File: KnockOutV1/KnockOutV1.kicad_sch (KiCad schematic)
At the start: 0 parts

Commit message: Added STM_Breakout and Documentation Files
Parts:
- added U1: STM32F103C8T6, STM32F103C8T6:QFP50P900X900X160-48N, symbol STM32F103C8T6:STM32F103C8T6
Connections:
- new net VDD: U1.24 (VDD), U1.36 (VDD), U1.48 (VDD)
- new net VSS: U1.23 (VSS), U1.35 (VSS), U1.47 (VSS)

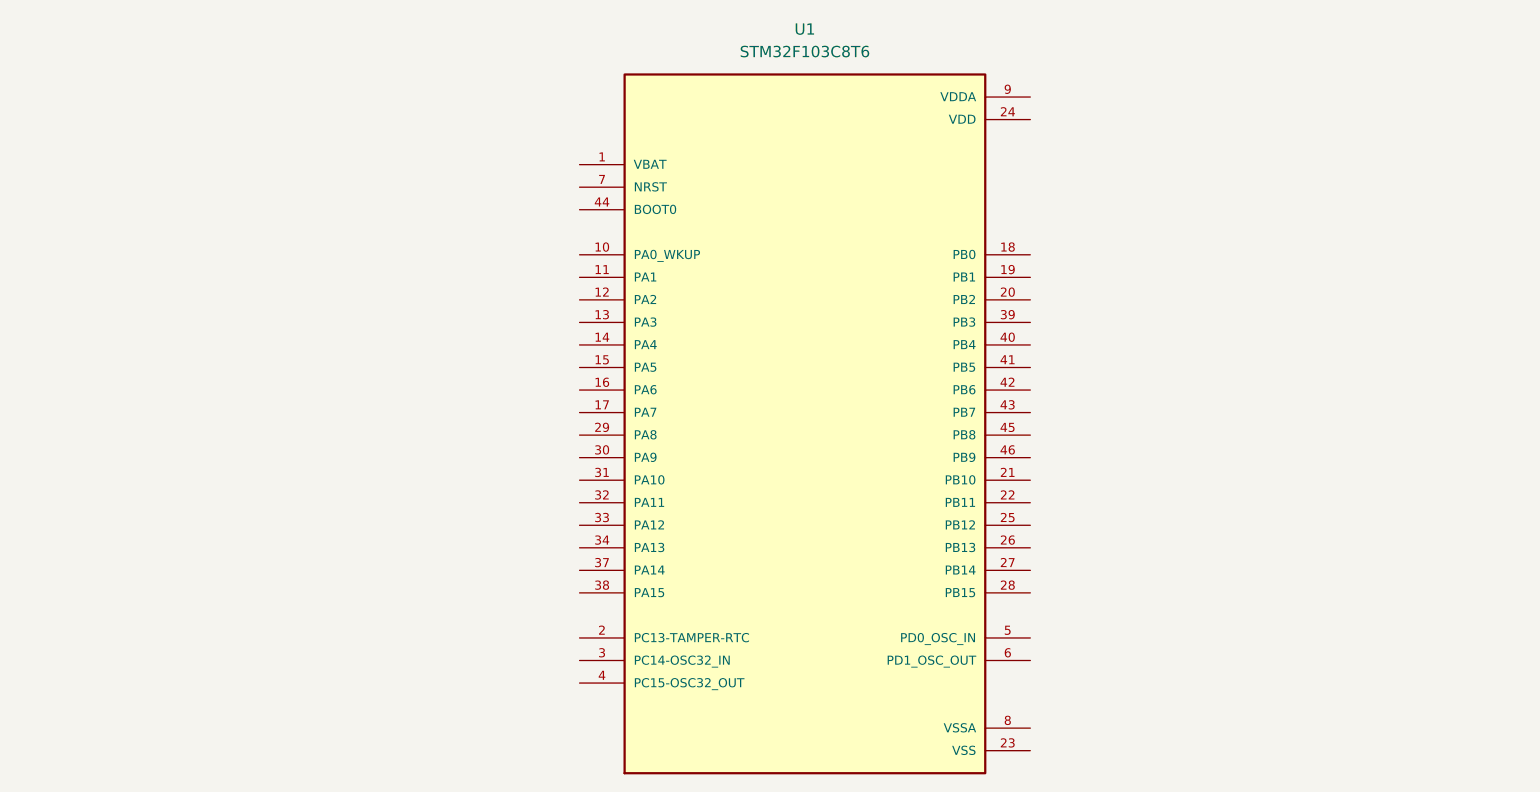
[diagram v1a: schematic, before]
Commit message: Began Schematic Pin Breakout
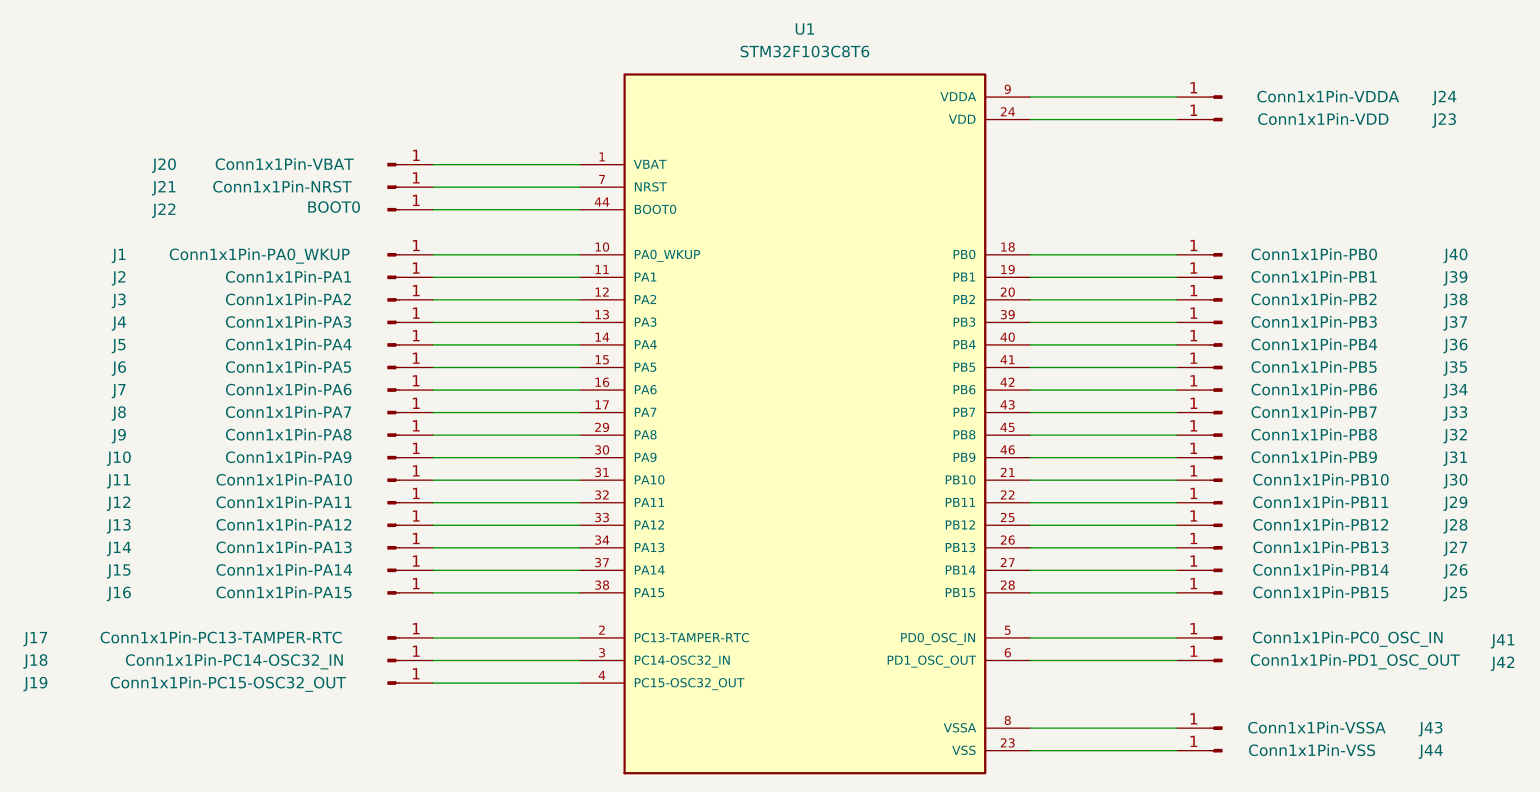
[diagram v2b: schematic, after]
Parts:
- added J1: Conn1x1Pin-PA0_WKUP, Connector_PinHeader_2.54mm:PinHeader_1x01_P2.54mm_Horizontal, symbol Connector:Conn_01x01_Pin
- added J10: Conn1x1Pin-PA9, Connector_PinHeader_2.54mm:PinHeader_1x01_P2.54mm_Horizontal, symbol Connector:Conn_01x01_Pin
- added J11: Conn1x1Pin-PA10, Connector_PinHeader_2.54mm:PinHeader_1x01_P2.54mm_Horizontal, symbol Connector:Conn_01x01_Pin
- added J12: Conn1x1Pin-PA11, Connector_PinHeader_2.54mm:PinHeader_1x01_P2.54mm_Horizontal, symbol Connector:Conn_01x01_Pin
- added J13: Conn1x1Pin-PA12, Connector_PinHeader_2.54mm:PinHeader_1x01_P2.54mm_Horizontal, symbol Connector:Conn_01x01_Pin
- added J14: Conn1x1Pin-PA13, Connector_PinHeader_2.54mm:PinHeader_1x01_P2.54mm_Horizontal, symbol Connector:Conn_01x01_Pin
- added J15: Conn1x1Pin-PA14, Connector_PinHeader_2.54mm:PinHeader_1x01_P2.54mm_Horizontal, symbol Connector:Conn_01x01_Pin
- added J16: Conn1x1Pin-PA15, Connector_PinHeader_2.54mm:PinHeader_1x01_P2.54mm_Horizontal, symbol Connector:Conn_01x01_Pin
- added J17: Conn1x1Pin-PC13-TAMPER-RTC, Connector_PinHeader_2.54mm:PinHeader_1x01_P2.54mm_Horizontal, symbol Connector:Conn_01x01_Pin
- added J18: Conn1x1Pin-PC14-OSC32_IN, Connector_PinHeader_2.54mm:PinHeader_1x01_P2.54mm_Horizontal, symbol Connector:Conn_01x01_Pin
- added J19: Conn1x1Pin-PC15-OSC32_OUT, Connector_PinHeader_2.54mm:PinHeader_1x01_P2.54mm_Horizontal, symbol Connector:Conn_01x01_Pin
- added J2: Conn1x1Pin-PA1, Connector_PinHeader_2.54mm:PinHeader_1x01_P2.54mm_Horizontal, symbol Connector:Conn_01x01_Pin
- added J20: Conn1x1Pin-VBAT, Connector_PinHeader_2.54mm:PinHeader_1x01_P2.54mm_Horizontal, symbol Connector:Conn_01x01_Pin
- added J21: Conn1x1Pin-NRST, Connector_PinHeader_2.54mm:PinHeader_1x01_P2.54mm_Horizontal, symbol Connector:Conn_01x01_Pin
- added J22: BOOT0, Connector_PinHeader_2.54mm:PinHeader_1x01_P2.54mm_Horizontal, symbol Connector:Conn_01x01_Pin
- added J23: Conn1x1Pin-VDD, Connector_PinHeader_2.54mm:PinHeader_1x01_P2.54mm_Horizontal, symbol Connector:Conn_01x01_Pin
- added J24: Conn1x1Pin-VDDA, Connector_PinHeader_2.54mm:PinHeader_1x01_P2.54mm_Horizontal, symbol Connector:Conn_01x01_Pin
- added J25: Conn1x1Pin-PB15, Connector_PinHeader_2.54mm:PinHeader_1x01_P2.54mm_Horizontal, symbol Connector:Conn_01x01_Pin
- added J26: Conn1x1Pin-PB14, Connector_PinHeader_2.54mm:PinHeader_1x01_P2.54mm_Horizontal, symbol Connector:Conn_01x01_Pin
- added J27: Conn1x1Pin-PB13, Connector_PinHeader_2.54mm:PinHeader_1x01_P2.54mm_Horizontal, symbol Connector:Conn_01x01_Pin
- added J28: Conn1x1Pin-PB12, Connector_PinHeader_2.54mm:PinHeader_1x01_P2.54mm_Horizontal, symbol Connector:Conn_01x01_Pin
- added J29: Conn1x1Pin-PB11, Connector_PinHeader_2.54mm:PinHeader_1x01_P2.54mm_Horizontal, symbol Connector:Conn_01x01_Pin
- added J3: Conn1x1Pin-PA2, Connector_PinHeader_2.54mm:PinHeader_1x01_P2.54mm_Horizontal, symbol Connector:Conn_01x01_Pin
- added J30: Conn1x1Pin-PB10, Connector_PinHeader_2.54mm:PinHeader_1x01_P2.54mm_Horizontal, symbol Connector:Conn_01x01_Pin
- added J31: Conn1x1Pin-PB9, Connector_PinHeader_2.54mm:PinHeader_1x01_P2.54mm_Horizontal, symbol Connector:Conn_01x01_Pin
- added J32: Conn1x1Pin-PB8, Connector_PinHeader_2.54mm:PinHeader_1x01_P2.54mm_Horizontal, symbol Connector:Conn_01x01_Pin
- added J33: Conn1x1Pin-PB7, Connector_PinHeader_2.54mm:PinHeader_1x01_P2.54mm_Horizontal, symbol Connector:Conn_01x01_Pin
- added J34: Conn1x1Pin-PB6, Connector_PinHeader_2.54mm:PinHeader_1x01_P2.54mm_Horizontal, symbol Connector:Conn_01x01_Pin
- added J35: Conn1x1Pin-PB5, Connector_PinHeader_2.54mm:PinHeader_1x01_P2.54mm_Horizontal, symbol Connector:Conn_01x01_Pin
- added J36: Conn1x1Pin-PB4, Connector_PinHeader_2.54mm:PinHeader_1x01_P2.54mm_Horizontal, symbol Connector:Conn_01x01_Pin
- added J37: Conn1x1Pin-PB3, Connector_PinHeader_2.54mm:PinHeader_1x01_P2.54mm_Horizontal, symbol Connector:Conn_01x01_Pin
- added J38: Conn1x1Pin-PB2, Connector_PinHeader_2.54mm:PinHeader_1x01_P2.54mm_Horizontal, symbol Connector:Conn_01x01_Pin
- added J39: Conn1x1Pin-PB1, Connector_PinHeader_2.54mm:PinHeader_1x01_P2.54mm_Horizontal, symbol Connector:Conn_01x01_Pin
- added J4: Conn1x1Pin-PA3, Connector_PinHeader_2.54mm:PinHeader_1x01_P2.54mm_Horizontal, symbol Connector:Conn_01x01_Pin
- added J40: Conn1x1Pin-PB0, Connector_PinHeader_2.54mm:PinHeader_1x01_P2.54mm_Horizontal, symbol Connector:Conn_01x01_Pin
- added J41: Conn1x1Pin-PC0_OSC_IN, Connector_PinHeader_2.54mm:PinHeader_1x01_P2.54mm_Horizontal, symbol Connector:Conn_01x01_Pin
- added J42: Conn1x1Pin-PD1_OSC_OUT, Connector_PinHeader_2.54mm:PinHeader_1x01_P2.54mm_Horizontal, symbol Connector:Conn_01x01_Pin
- added J43: Conn1x1Pin-VSSA, Connector_PinHeader_2.54mm:PinHeader_1x01_P2.54mm_Horizontal, symbol Connector:Conn_01x01_Pin
- added J44: Conn1x1Pin-VSS, Connector_PinHeader_2.54mm:PinHeader_1x01_P2.54mm_Horizontal, symbol Connector:Conn_01x01_Pin
- added J5: Conn1x1Pin-PA4, Connector_PinHeader_2.54mm:PinHeader_1x01_P2.54mm_Horizontal, symbol Connector:Conn_01x01_Pin
- added J6: Conn1x1Pin-PA5, Connector_PinHeader_2.54mm:PinHeader_1x01_P2.54mm_Horizontal, symbol Connector:Conn_01x01_Pin
- added J7: Conn1x1Pin-PA6, Connector_PinHeader_2.54mm:PinHeader_1x01_P2.54mm_Horizontal, symbol Connector:Conn_01x01_Pin
- added J8: Conn1x1Pin-PA7, Connector_PinHeader_2.54mm:PinHeader_1x01_P2.54mm_Horizontal, symbol Connector:Conn_01x01_Pin
- added J9: Conn1x1Pin-PA8, Connector_PinHeader_2.54mm:PinHeader_1x01_P2.54mm_Horizontal, symbol Connector:Conn_01x01_Pin
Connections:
- net VDD: now also J23.1 (Pin_1)
- net VSS: now also J44.1 (Pin_1)
- net at U1.1 (VBAT): now also J20.1 (Pin_1)
- net at U1.10 (PA0_WKUP): now also J1.1 (Pin_1)
- net at U1.11 (PA1): now also J2.1 (Pin_1)
- net at U1.12 (PA2): now also J3.1 (Pin_1)
- net at U1.13 (PA3): now also J4.1 (Pin_1)
- net at U1.14 (PA4): now also J5.1 (Pin_1)
- net at U1.15 (PA5): now also J6.1 (Pin_1)
- net at U1.16 (PA6): now also J7.1 (Pin_1)
- net at U1.17 (PA7): now also J8.1 (Pin_1)
- net at U1.18 (PB0): now also J40.1 (Pin_1)
- net at U1.19 (PB1): now also J39.1 (Pin_1)
- net at U1.2 (PC13-TAMPER-RTC): now also J17.1 (Pin_1)
- net at U1.20 (PB2): now also J38.1 (Pin_1)
- net at U1.21 (PB10): now also J30.1 (Pin_1)
- net at U1.22 (PB11): now also J29.1 (Pin_1)
- net at U1.25 (PB12): now also J28.1 (Pin_1)
- net at U1.26 (PB13): now also J27.1 (Pin_1)
- net at U1.27 (PB14): now also J26.1 (Pin_1)
- net at U1.28 (PB15): now also J25.1 (Pin_1)
- net at U1.29 (PA8): now also J9.1 (Pin_1)
- net at U1.3 (PC14-OSC32_IN): now also J18.1 (Pin_1)
- net at U1.30 (PA9): now also J10.1 (Pin_1)
- net at U1.31 (PA10): now also J11.1 (Pin_1)
- net at U1.32 (PA11): now also J12.1 (Pin_1)
- net at U1.33 (PA12): now also J13.1 (Pin_1)
- net at U1.34 (PA13): now also J14.1 (Pin_1)
- net at U1.37 (PA14): now also J15.1 (Pin_1)
- net at U1.38 (PA15): now also J16.1 (Pin_1)
- net at U1.39 (PB3): now also J37.1 (Pin_1)
- net at U1.4 (PC15-OSC32_OUT): now also J19.1 (Pin_1)
- net at U1.40 (PB4): now also J36.1 (Pin_1)
- net at U1.41 (PB5): now also J35.1 (Pin_1)
- net at U1.42 (PB6): now also J34.1 (Pin_1)
- net at U1.43 (PB7): now also J33.1 (Pin_1)
- net at U1.44 (BOOT0): now also J22.1 (Pin_1)
- net at U1.45 (PB8): now also J32.1 (Pin_1)
- net at U1.46 (PB9): now also J31.1 (Pin_1)
- net at U1.5 (PD0_OSC_IN): now also J41.1 (Pin_1)
- net at U1.6 (PD1_OSC_OUT): now also J42.1 (Pin_1)
- net at U1.7 (NRST): now also J21.1 (Pin_1)
- net at U1.8 (VSSA): now also J43.1 (Pin_1)
- net at U1.9 (VDDA): now also J24.1 (Pin_1)

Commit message: Rearraged Files
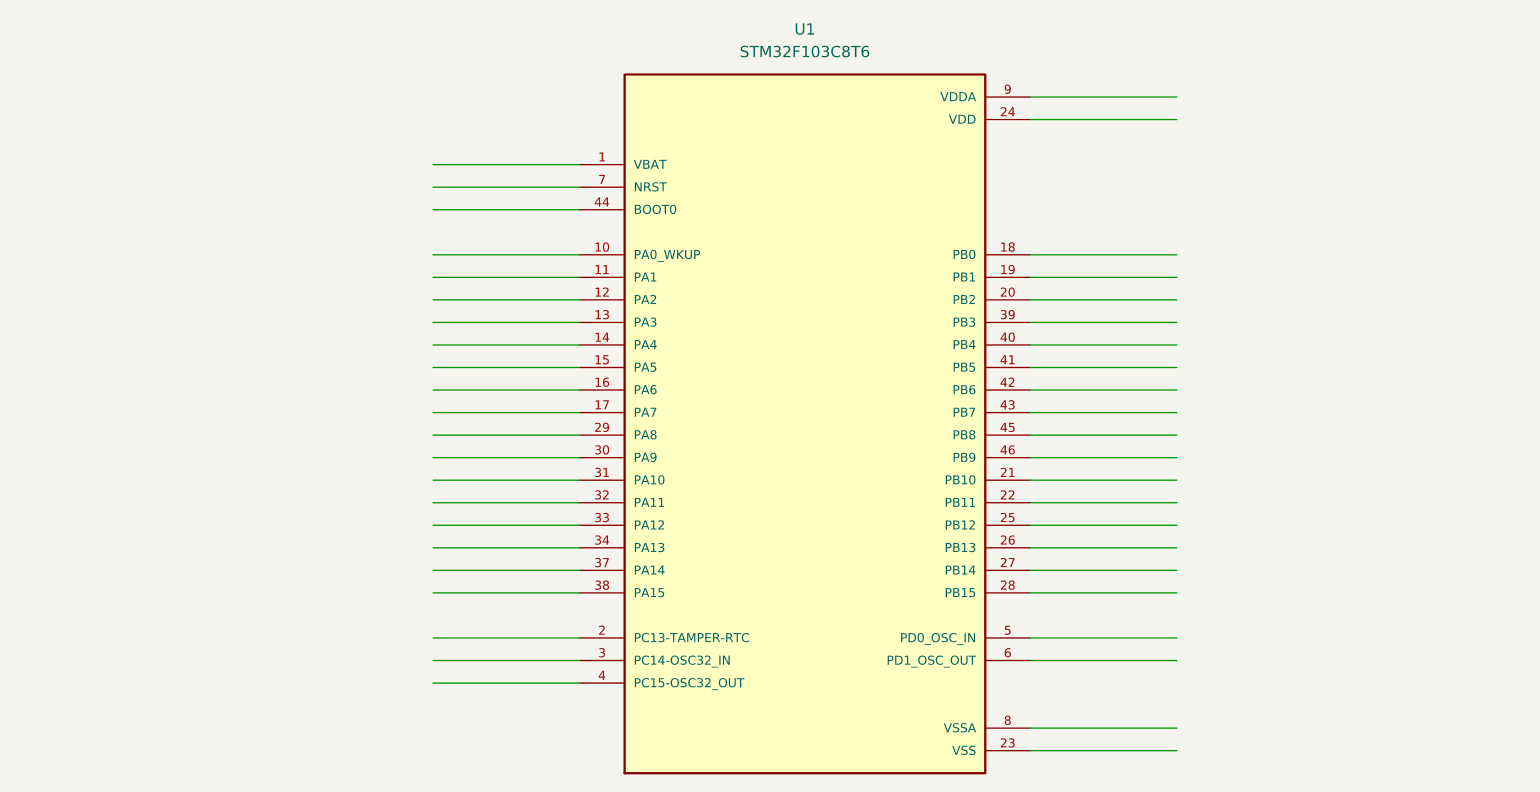
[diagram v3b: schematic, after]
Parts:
- removed J1: Conn1x1Pin-PA0_WKUP, Connector_PinHeader_2.54mm:PinHeader_1x01_P2.54mm_Horizontal, symbol Connector:Conn_01x01_Pin
- removed J10: Conn1x1Pin-PA9, Connector_PinHeader_2.54mm:PinHeader_1x01_P2.54mm_Horizontal, symbol Connector:Conn_01x01_Pin
- removed J11: Conn1x1Pin-PA10, Connector_PinHeader_2.54mm:PinHeader_1x01_P2.54mm_Horizontal, symbol Connector:Conn_01x01_Pin
- removed J12: Conn1x1Pin-PA11, Connector_PinHeader_2.54mm:PinHeader_1x01_P2.54mm_Horizontal, symbol Connector:Conn_01x01_Pin
- removed J13: Conn1x1Pin-PA12, Connector_PinHeader_2.54mm:PinHeader_1x01_P2.54mm_Horizontal, symbol Connector:Conn_01x01_Pin
- removed J14: Conn1x1Pin-PA13, Connector_PinHeader_2.54mm:PinHeader_1x01_P2.54mm_Horizontal, symbol Connector:Conn_01x01_Pin
- removed J15: Conn1x1Pin-PA14, Connector_PinHeader_2.54mm:PinHeader_1x01_P2.54mm_Horizontal, symbol Connector:Conn_01x01_Pin
- removed J16: Conn1x1Pin-PA15, Connector_PinHeader_2.54mm:PinHeader_1x01_P2.54mm_Horizontal, symbol Connector:Conn_01x01_Pin
- removed J17: Conn1x1Pin-PC13-TAMPER-RTC, Connector_PinHeader_2.54mm:PinHeader_1x01_P2.54mm_Horizontal, symbol Connector:Conn_01x01_Pin
- removed J18: Conn1x1Pin-PC14-OSC32_IN, Connector_PinHeader_2.54mm:PinHeader_1x01_P2.54mm_Horizontal, symbol Connector:Conn_01x01_Pin
- removed J19: Conn1x1Pin-PC15-OSC32_OUT, Connector_PinHeader_2.54mm:PinHeader_1x01_P2.54mm_Horizontal, symbol Connector:Conn_01x01_Pin
- removed J2: Conn1x1Pin-PA1, Connector_PinHeader_2.54mm:PinHeader_1x01_P2.54mm_Horizontal, symbol Connector:Conn_01x01_Pin
- removed J20: Conn1x1Pin-VBAT, Connector_PinHeader_2.54mm:PinHeader_1x01_P2.54mm_Horizontal, symbol Connector:Conn_01x01_Pin
- removed J21: Conn1x1Pin-NRST, Connector_PinHeader_2.54mm:PinHeader_1x01_P2.54mm_Horizontal, symbol Connector:Conn_01x01_Pin
- removed J22: BOOT0, Connector_PinHeader_2.54mm:PinHeader_1x01_P2.54mm_Horizontal, symbol Connector:Conn_01x01_Pin
- removed J23: Conn1x1Pin-VDD, Connector_PinHeader_2.54mm:PinHeader_1x01_P2.54mm_Horizontal, symbol Connector:Conn_01x01_Pin
- removed J24: Conn1x1Pin-VDDA, Connector_PinHeader_2.54mm:PinHeader_1x01_P2.54mm_Horizontal, symbol Connector:Conn_01x01_Pin
- removed J25: Conn1x1Pin-PB15, Connector_PinHeader_2.54mm:PinHeader_1x01_P2.54mm_Horizontal, symbol Connector:Conn_01x01_Pin
- removed J26: Conn1x1Pin-PB14, Connector_PinHeader_2.54mm:PinHeader_1x01_P2.54mm_Horizontal, symbol Connector:Conn_01x01_Pin
- removed J27: Conn1x1Pin-PB13, Connector_PinHeader_2.54mm:PinHeader_1x01_P2.54mm_Horizontal, symbol Connector:Conn_01x01_Pin
- removed J28: Conn1x1Pin-PB12, Connector_PinHeader_2.54mm:PinHeader_1x01_P2.54mm_Horizontal, symbol Connector:Conn_01x01_Pin
- removed J29: Conn1x1Pin-PB11, Connector_PinHeader_2.54mm:PinHeader_1x01_P2.54mm_Horizontal, symbol Connector:Conn_01x01_Pin
- removed J3: Conn1x1Pin-PA2, Connector_PinHeader_2.54mm:PinHeader_1x01_P2.54mm_Horizontal, symbol Connector:Conn_01x01_Pin
- removed J30: Conn1x1Pin-PB10, Connector_PinHeader_2.54mm:PinHeader_1x01_P2.54mm_Horizontal, symbol Connector:Conn_01x01_Pin
- removed J31: Conn1x1Pin-PB9, Connector_PinHeader_2.54mm:PinHeader_1x01_P2.54mm_Horizontal, symbol Connector:Conn_01x01_Pin
- removed J32: Conn1x1Pin-PB8, Connector_PinHeader_2.54mm:PinHeader_1x01_P2.54mm_Horizontal, symbol Connector:Conn_01x01_Pin
- removed J33: Conn1x1Pin-PB7, Connector_PinHeader_2.54mm:PinHeader_1x01_P2.54mm_Horizontal, symbol Connector:Conn_01x01_Pin
- removed J34: Conn1x1Pin-PB6, Connector_PinHeader_2.54mm:PinHeader_1x01_P2.54mm_Horizontal, symbol Connector:Conn_01x01_Pin
- removed J35: Conn1x1Pin-PB5, Connector_PinHeader_2.54mm:PinHeader_1x01_P2.54mm_Horizontal, symbol Connector:Conn_01x01_Pin
- removed J36: Conn1x1Pin-PB4, Connector_PinHeader_2.54mm:PinHeader_1x01_P2.54mm_Horizontal, symbol Connector:Conn_01x01_Pin
- removed J37: Conn1x1Pin-PB3, Connector_PinHeader_2.54mm:PinHeader_1x01_P2.54mm_Horizontal, symbol Connector:Conn_01x01_Pin
- removed J38: Conn1x1Pin-PB2, Connector_PinHeader_2.54mm:PinHeader_1x01_P2.54mm_Horizontal, symbol Connector:Conn_01x01_Pin
- removed J39: Conn1x1Pin-PB1, Connector_PinHeader_2.54mm:PinHeader_1x01_P2.54mm_Horizontal, symbol Connector:Conn_01x01_Pin
- removed J4: Conn1x1Pin-PA3, Connector_PinHeader_2.54mm:PinHeader_1x01_P2.54mm_Horizontal, symbol Connector:Conn_01x01_Pin
- removed J40: Conn1x1Pin-PB0, Connector_PinHeader_2.54mm:PinHeader_1x01_P2.54mm_Horizontal, symbol Connector:Conn_01x01_Pin
- removed J41: Conn1x1Pin-PC0_OSC_IN, Connector_PinHeader_2.54mm:PinHeader_1x01_P2.54mm_Horizontal, symbol Connector:Conn_01x01_Pin
- removed J42: Conn1x1Pin-PD1_OSC_OUT, Connector_PinHeader_2.54mm:PinHeader_1x01_P2.54mm_Horizontal, symbol Connector:Conn_01x01_Pin
- removed J43: Conn1x1Pin-VSSA, Connector_PinHeader_2.54mm:PinHeader_1x01_P2.54mm_Horizontal, symbol Connector:Conn_01x01_Pin
- removed J44: Conn1x1Pin-VSS, Connector_PinHeader_2.54mm:PinHeader_1x01_P2.54mm_Horizontal, symbol Connector:Conn_01x01_Pin
- removed J5: Conn1x1Pin-PA4, Connector_PinHeader_2.54mm:PinHeader_1x01_P2.54mm_Horizontal, symbol Connector:Conn_01x01_Pin
- removed J6: Conn1x1Pin-PA5, Connector_PinHeader_2.54mm:PinHeader_1x01_P2.54mm_Horizontal, symbol Connector:Conn_01x01_Pin
- removed J7: Conn1x1Pin-PA6, Connector_PinHeader_2.54mm:PinHeader_1x01_P2.54mm_Horizontal, symbol Connector:Conn_01x01_Pin
- removed J8: Conn1x1Pin-PA7, Connector_PinHeader_2.54mm:PinHeader_1x01_P2.54mm_Horizontal, symbol Connector:Conn_01x01_Pin
- removed J9: Conn1x1Pin-PA8, Connector_PinHeader_2.54mm:PinHeader_1x01_P2.54mm_Horizontal, symbol Connector:Conn_01x01_Pin

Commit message: Added to Schematics
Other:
- added sheet PiezoOut (PiezoOut.kicad_sch)
- moved on the sheet: U1
